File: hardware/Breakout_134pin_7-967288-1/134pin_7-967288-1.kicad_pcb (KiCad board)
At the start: 2 copper layers, 0 parts

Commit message: draft3
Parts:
- added REF**: 7-967288-1_134-pin-connector, Breakout_134pin_7-967288-1_KC5:7-967288-1_134-pin-connector, F.Cu at (69.3, 110.0)

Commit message: 134 board
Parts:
- removed REF**: 7-967288-1_134-pin-connector, Breakout_134pin_7-967288-1_KC5:7-967288-1_134-pin-connector
- added J1: Conn_01x03, Connector_Phoenix_MSTB:PhoenixContact_MSTBA_2,5_3-G-5,08_1x03_P5.08mm_Horizontal, F.Cu at (89.5, 99.7)
- added J10: Conn_01x06, Connector_PinHeader_2.54mm:PinHeader_1x06_P2.54mm_Vertical, F.Cu at (106.7, 78.1)
- added J11: Conn_01x06, Connector_PinHeader_2.54mm:PinHeader_1x06_P2.54mm_Vertical, F.Cu at (106.7, 68.6)
- added J12: Conn_01x03, Connector_Phoenix_MSTB:PhoenixContact_MSTBA_2,5_3-G-5,08_1x03_P5.08mm_Horizontal, F.Cu at (89.5, 95.2)
- added J13: Conn_01x03, Connector_Phoenix_MSTB:PhoenixContact_MSTBA_2,5_3-G-5,08_1x03_P5.08mm_Horizontal, F.Cu at (89.5, 83.2)
- added J14: Conn_01x03, Connector_Phoenix_MSTB:PhoenixContact_MSTBA_2,5_3-G-5,08_1x03_P5.08mm_Horizontal, F.Cu at (89.5, 71.1)
- added J15: Conn_01x13, Connector_PinHeader_2.54mm:PinHeader_1x13_P2.54mm_Vertical, F.Cu at (124.5, 100.3)
- added J16: Conn_01x13, Connector_PinHeader_2.54mm:PinHeader_1x13_P2.54mm_Vertical, F.Cu at (124.5, 90.8)
- added J17: Conn_01x13, Connector_PinHeader_2.54mm:PinHeader_1x13_P2.54mm_Vertical, F.Cu at (125.1, 81.3)
- added J18: Conn_01x13, Connector_PinHeader_2.54mm:PinHeader_1x13_P2.54mm_Vertical, F.Cu at (124.5, 71.8)
- added J19: Conn_01x13, Connector_PinHeader_2.54mm:PinHeader_1x13_P2.54mm_Vertical, F.Cu at (124.5, 97.2)
- added J2: Conn_01x03, Connector_Phoenix_MSTB:PhoenixContact_MSTBA_2,5_3-G-5,08_1x03_P5.08mm_Horizontal, F.Cu at (89.5, 87.6)
- added J20: Conn_01x13, Connector_PinHeader_2.54mm:PinHeader_1x13_P2.54mm_Vertical, F.Cu at (124.5, 87.6)
- added J21: Conn_01x13, Connector_PinHeader_2.54mm:PinHeader_1x13_P2.54mm_Vertical, F.Cu at (125.1, 78.1)
- added J22: Conn_01x13, Connector_PinHeader_2.54mm:PinHeader_1x13_P2.54mm_Vertical, F.Cu at (124.5, 68.6)
- added J23: Conn_01x10, Connector_PinHeader_2.54mm:PinHeader_1x10_P2.54mm_Vertical, F.Cu at (161.3, 100.3)
- added J24: Conn_01x10, Connector_PinHeader_2.54mm:PinHeader_1x10_P2.54mm_Vertical, F.Cu at (161.3, 87.6)
- added J25: Conn_01x10, Connector_PinHeader_2.54mm:PinHeader_1x10_P2.54mm_Vertical, F.Cu at (161.3, 78.1)
- added J26: Conn_01x10, Connector_PinHeader_2.54mm:PinHeader_1x10_P2.54mm_Vertical, F.Cu at (161.3, 68.6)
- added J27: Conn_01x03, Connector_Phoenix_MSTB:PhoenixContact_MSTBA_2,5_3-G-5,08_1x03_P5.08mm_Horizontal, F.Cu at (191.1, 95.2)
- added J28: Conn_01x03, Connector_Phoenix_MSTB:PhoenixContact_MSTBA_2,5_3-G-5,08_1x03_P5.08mm_Horizontal, F.Cu at (191.1, 83.2)
- added J29: Conn_01x03, Connector_Phoenix_MSTB:PhoenixContact_MSTBA_2,5_3-G-5,08_1x03_P5.08mm_Horizontal, F.Cu at (191.1, 71.8)
- added J3: Conn_01x03, Connector_Phoenix_MSTB:PhoenixContact_MSTBA_2,5_3-G-5,08_1x03_P5.08mm_Horizontal, F.Cu at (89.5, 75.6)
- added J30: Conn_01x10, Connector_PinHeader_2.54mm:PinHeader_1x10_P2.54mm_Vertical, F.Cu at (161.3, 97.2)
- added J31: Conn_01x10, Connector_PinHeader_2.54mm:PinHeader_1x10_P2.54mm_Vertical, F.Cu at (161.3, 90.8)
- added J32: Conn_01x10, Connector_PinHeader_2.54mm:PinHeader_1x10_P2.54mm_Vertical, F.Cu at (161.3, 81.3)
- added J33: Conn_01x10, Connector_PinHeader_2.54mm:PinHeader_1x10_P2.54mm_Vertical, F.Cu at (161.3, 71.8)
- added J34: Conn_01x03, Connector_Phoenix_MSTB:PhoenixContact_MSTBA_2,5_3-G-5,08_1x03_P5.08mm_Horizontal, F.Cu at (191.1, 100.3)
- added J35: Conn_01x03, Connector_Phoenix_MSTB:PhoenixContact_MSTBA_2,5_3-G-5,08_1x03_P5.08mm_Horizontal, F.Cu at (191.1, 88.3)
- added J36: Conn_01x03, Connector_Phoenix_MSTB:PhoenixContact_MSTBA_2,5_3-G-5,08_1x03_P5.08mm_Horizontal, F.Cu at (191.1, 76.2)
- added J4: Conn_01x06, Connector_PinHeader_2.54mm:PinHeader_1x06_P2.54mm_Vertical, F.Cu at (106.7, 100.3)
- added J5: Conn_01x06, Connector_PinHeader_2.54mm:PinHeader_1x06_P2.54mm_Vertical, F.Cu at (106.7, 90.8)
- added J6: Conn_01x06, Connector_PinHeader_2.54mm:PinHeader_1x06_P2.54mm_Vertical, F.Cu at (106.7, 81.3)
- added J7: Conn_01x06, Connector_PinHeader_2.54mm:PinHeader_1x06_P2.54mm_Vertical, F.Cu at (106.7, 71.8)
- added J8: Conn_01x06, Connector_PinHeader_2.54mm:PinHeader_1x06_P2.54mm_Vertical, F.Cu at (106.7, 97.2)
- added J9: Conn_01x06, Connector_PinHeader_2.54mm:PinHeader_1x06_P2.54mm_Vertical, F.Cu at (106.7, 87.6)
- added LOGO1: DNP, rusEFI:LOGO, F.Cu at (210.8, 104.1)
- added LOGO2: DNP, Symbol:OSHW-Logo2_7.3x6mm_SilkScreen, F.Cu at (81.3, 104.1)
- added P1: 134pin_7-967288-1_KC5, 134pin_7-967288-1_KC5_FOOTPRINT:7-967288-1_134-pin-connector, F.Cu at (80.6, 125.1)
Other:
- board outline added: 139.7 x 73.7 mm

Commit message: update
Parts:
- added J37: Conn_01x01, TestPoint:TestPoint_Keystone_5000-5004_Miniature, F.Cu at (78.7, 83.8)
- moved J15 28.6 mm to (125.1, 71.8)
- moved J18 28.6 mm to (125.1, 100.3)
- moved J19 28.6 mm to (125.1, 68.6)
- moved J22 28.6 mm to (125.1, 97.2)
- moved J11 28.6 mm to (106.7, 97.2)
- moved J23 28.6 mm to (161.3, 71.8)
- moved J26 28.6 mm to (161.3, 97.2)
- moved J30 28.6 mm to (161.3, 68.6)
- moved J33 28.6 mm to (161.3, 100.3)
- moved J4 28.6 mm to (106.7, 71.8)
- moved J7 28.6 mm to (106.7, 100.3)
- moved J8 28.6 mm to (106.7, 68.6)
- moved J27 25.4 mm to (191.8, 69.8)
- moved J34 25.4 mm to (191.8, 74.9)
- moved J12 25.4 mm to (89.5, 69.8)
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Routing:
- net Net-(J23-Pad1): track 0.00 -> 114.2 mm, vias 0 -> 1
- net Net-(J23-Pad2): track 0.00 -> 107.4 mm, vias 0 -> 1
- net Net-(J23-Pad3): track 0.00 -> 101.6 mm, vias 0 -> 1
- net Net-(J23-Pad4): track 0.00 -> 96.0 mm, vias 0 -> 1
- net Net-(J15-Pad7): track 0.00 -> 95.8 mm, vias 0 -> 1
- net Net-(J15-Pad8): track 0.00 -> 89.9 mm, vias 0 -> 1
- net Net-(J23-Pad5): track 0.00 -> 89.7 mm, vias 0 -> 1
- net Net-(J15-Pad6): track 0.00 -> 89.5 mm, vias 0 -> 1
- net Net-(J4-Pad6): track 0.00 -> 88.7 mm, vias 0 -> 1
- net Net-(J15-Pad9): track 0.00 -> 83.5 mm, vias 0 -> 1
- net Net-(J23-Pad6): track 0.00 -> 83.4 mm, vias 0 -> 1
- net Net-(J15-Pad5): track 0.00 -> 83.3 mm, vias 0 -> 1
- net Net-(J4-Pad5): track 0.00 -> 82.8 mm, vias 0 -> 1
- net Net-(J23-Pad7): track 0.00 -> 77.0 mm, vias 0 -> 1
- net Net-(J15-Pad10): track 0.00 -> 77.0 mm, vias 0 -> 1
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- added copper zone on B.Cu, net (none)
- added copper zone on F.Cu, net GND
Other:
- outline, holes or cut-outs redrawn
- rule trace_min: 0.2032 -> 0.1524
- board text added: "rusEFI.com 134pin 7-967288-1 R0.1"

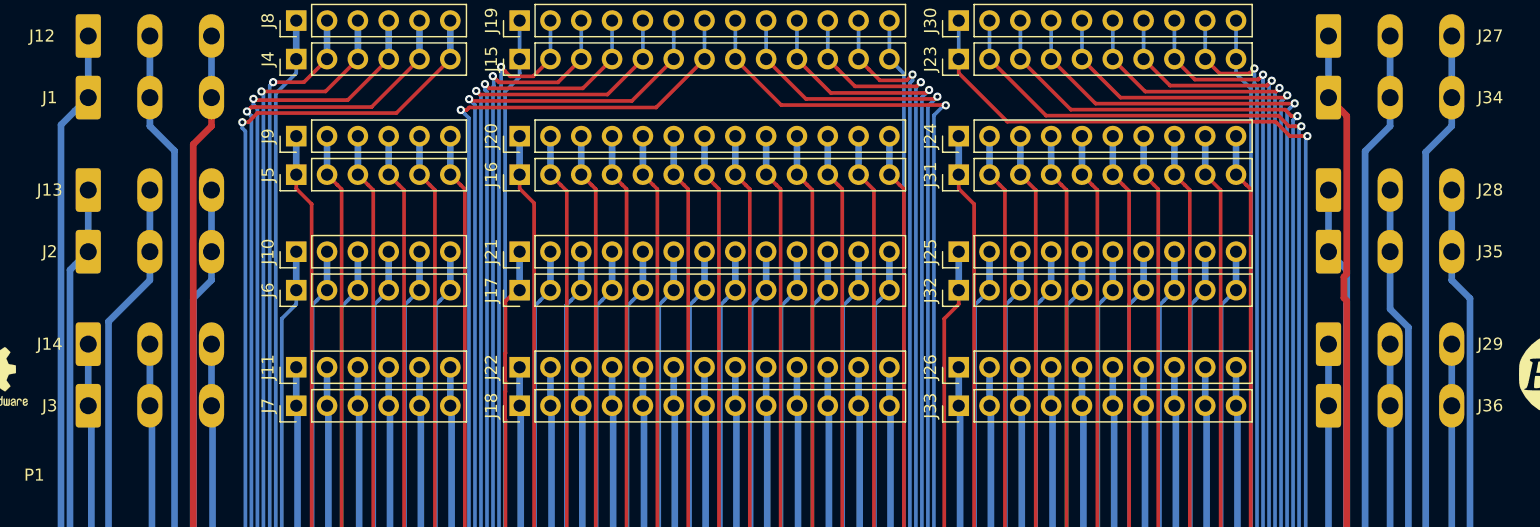
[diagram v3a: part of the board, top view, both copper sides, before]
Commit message: more silkscreen
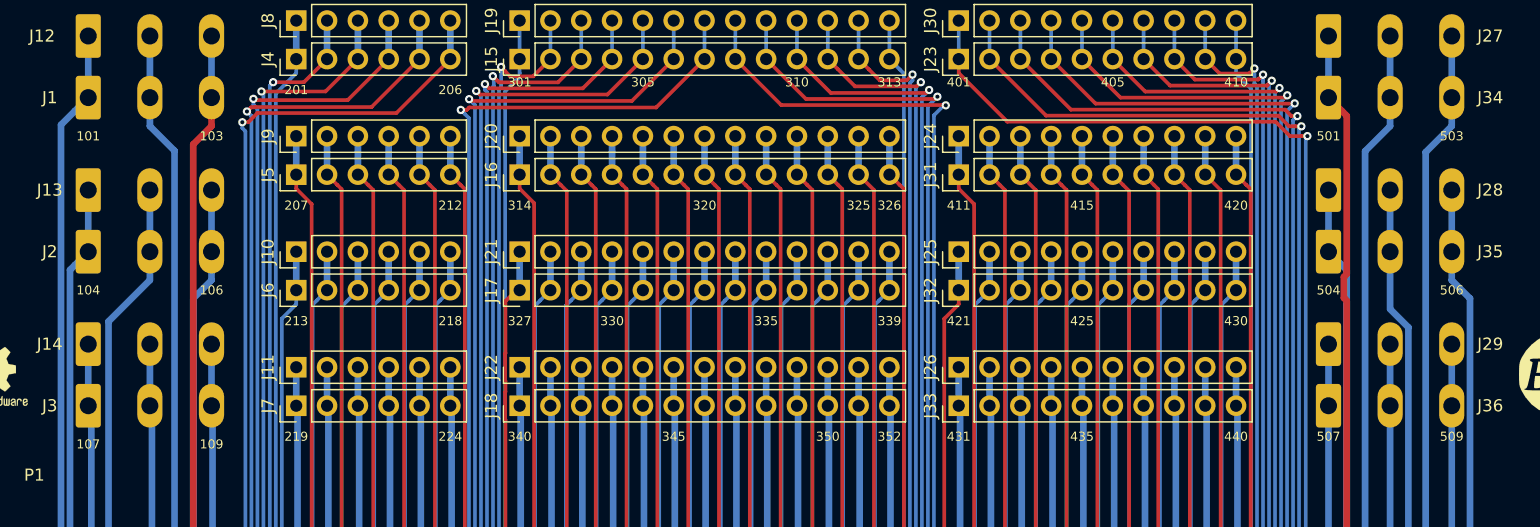
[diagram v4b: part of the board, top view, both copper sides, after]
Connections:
- net Net-(J1-Pad1) renamed /101
- net Net-(J1-Pad3) renamed /103
- net Net-(J10-Pad1) renamed /213
- net Net-(J10-Pad6) renamed /218
- net Net-(J11-Pad1) renamed /219
- net Net-(J11-Pad6) renamed /224
- net Net-(J13-Pad1) renamed /104
- net Net-(J13-Pad3) renamed /106
- net Net-(J14-Pad1) renamed /107
- net Net-(J14-Pad3) renamed /109
- net Net-(J15-Pad1) renamed /301
- net Net-(J15-Pad10) renamed /310
- net Net-(J15-Pad13) renamed /313
- net Net-(J15-Pad5) renamed /305
- net Net-(J16-Pad1) renamed /314
- net Net-(J16-Pad12) renamed /325
- net Net-(J16-Pad13) renamed /326
- net Net-(J16-Pad2) renamed /315
- net Net-(J16-Pad7) renamed /320
- net Net-(J17-Pad1) renamed /327
- net Net-(J17-Pad13) renamed /339
- net Net-(J17-Pad4) renamed /330
- net Net-(J17-Pad9) renamed /335
- net Net-(J18-Pad1) renamed /340
- net Net-(J18-Pad11) renamed /350
- net Net-(J18-Pad13) renamed /352
- net Net-(J18-Pad6) renamed /345
- net Net-(J23-Pad1) renamed /401
- net Net-(J23-Pad10) renamed /410
- net Net-(J23-Pad5) renamed /405
- net Net-(J24-Pad1) renamed /411
- net Net-(J24-Pad10) renamed /420
- net Net-(J24-Pad5) renamed /415
- net Net-(J25-Pad1) renamed /421
- net Net-(J25-Pad10) renamed /430
- net Net-(J25-Pad5) renamed /425
- net Net-(J26-Pad1) renamed /431
- net Net-(J26-Pad10) renamed /440
- net Net-(J26-Pad5) renamed /435
- net Net-(J27-Pad1) renamed /501
- net Net-(J27-Pad3) renamed /503
- net Net-(J28-Pad1) renamed /504
- net Net-(J28-Pad3) renamed /506
- net Net-(J29-Pad1) renamed /507
- net Net-(J29-Pad3) renamed /509
- net Net-(J4-Pad1) renamed /201
- net Net-(J4-Pad6) renamed /206
- net Net-(J5-Pad1) renamed /207
- net Net-(J5-Pad6) renamed /212
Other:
- board text added: "101"
- board text added: "103"
- board text added: "104"
- board text added: "106"
- board text added: "107"
- board text added: "109"
- board text added: "201"
- board text added: "206"
- board text added: "207"
- board text added: "212"
- board text added: "213"
- board text added: "218"
- board text added: "219"
- board text added: "224"
- board text added: "301"
- board text added: "305"
- board text added: "310"
- board text added: "313"
- board text added: "314"
- board text added: "320"
- board text added: "325"
- board text added: "326"
- board text added: "327"
- board text added: "330"
- board text added: "335"
- board text added: "339"
- board text added: "340"
- board text added: "345"
- board text added: "350"
- board text added: "352"
- board text added: "401"
- board text added: "405"
- board text added: "410"
- board text added: "411"
- board text added: "415"
- board text added: "420"
- board text added: "421"
- board text added: "425"
- board text added: "430"
- board text added: "431"
- board text added: "435"
- board text added: "440"
- board text added: "501"
- board text added: "503"
- board text added: "504"
- board text added: "506"
- board text added: "507"
- board text added: "509"
